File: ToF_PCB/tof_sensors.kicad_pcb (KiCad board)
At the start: 2 copper layers, 80 x 14 mm, 22 parts, among them J1 Conn_01x06, Q1 2N7002, Q2 2N7002, U1 LP5907MFX-2.8, U2 VL53L4CD, U3 VL53L4CD

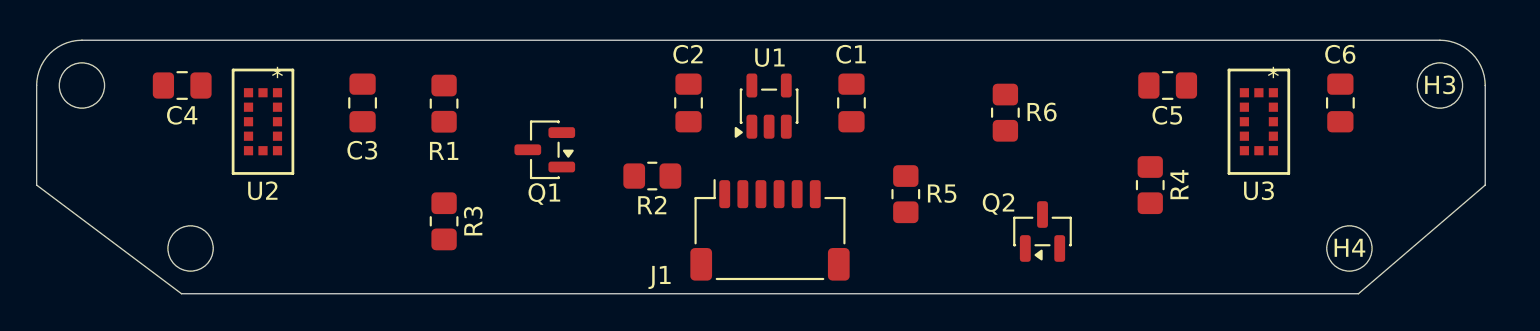
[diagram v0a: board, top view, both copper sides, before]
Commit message: Added layers and fixed layout + shape of pcb. Going to add esd protection now so pushing changes before doing so.
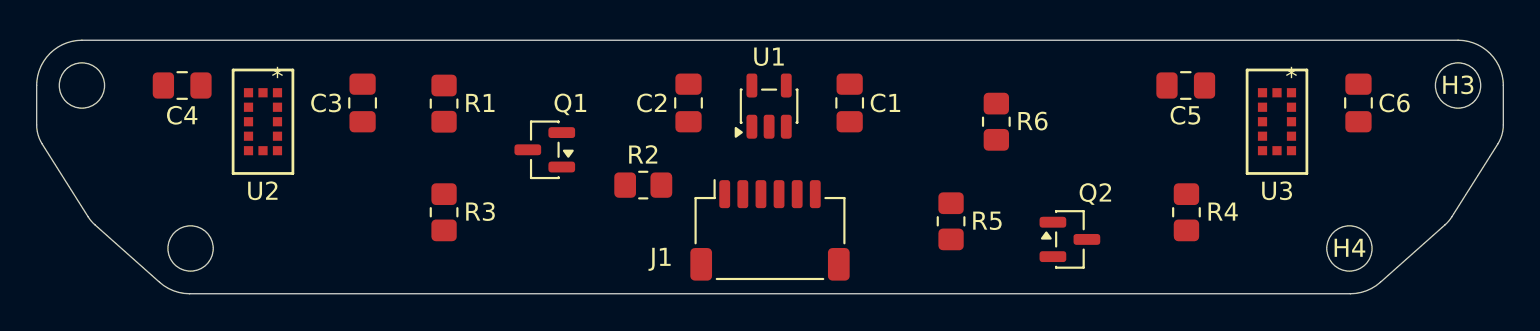
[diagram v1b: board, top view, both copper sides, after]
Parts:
- moved R5 2.92 mm to (132.0, 40.0)
- moved R4 2.50 mm to (145.0, 39.5)
- moved Q2 1.57 mm to (138.6, 41.0), turned to 0 degrees
- moved C5 1.00 mm to (145.0, 32.5)
- moved C6 1.00 mm to (154.5, 33.5)
- moved H3 1.00 mm to (160.0, 32.5)
- moved U3 1.00 mm to (150.0, 34.5)
- moved R2 0.71 mm to (115.0, 38.0)
- moved R6 0.71 mm to (134.5, 34.5), turned to 90 degrees
- moved R3 0.50 mm to (104.0, 39.5)
- moved C1 0.10 mm to (126.4, 33.5)
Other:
- board size 80 x 14 mm -> 81 x 14 mm
- copper layers 2 -> 4

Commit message: Updated pcb layout. Moved ToF sensors to back of board.
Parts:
- added C7: 100nF, Capacitor_SMD:C_0402_1005Metric, F.Cu at (126.3, 36.2)
- added U4: USBLC6-4SC6, Package_TO_SOT_SMD:SOT-23-6, F.Cu at (129.4, 36.3)
- C1, C2: footprint Capacitor_SMD:C_0805_2012Metric_Pad1.18x1.45mm_HandSolder -> Capacitor_SMD:C_0603_1608Metric_Pad1.08x0.95mm_HandSolder
- J1: footprint Connector_JST:JST_SH_SM06B-SRSS-TB_1x06-1MP_P1.00mm_Horizontal -> Connector_JST:JST_SH_BM06B-SRSS-TB_1x06-1MP_P1.00mm_Vertical
- U2, U3: moved to B.Cu
- moved R3 33.5 mm to (137.0, 33.5)
- moved R6 18.0 mm to (116.5, 33.5)
- moved R1 14.5 mm to (89.5, 32.5)
- moved C1 11.7 mm to (116.5, 39.9)
- moved Q1 11.5 mm to (99.0, 40.5)
- moved R2 10.9 mm to (104.4, 40.5), turned to -90 degrees
- moved C5 10.5 mm to (155.2, 34.5), turned to 0 degrees
- moved C4 10.0 mm to (99.5, 32.0), turned to 0 degrees
- moved U1 9.82 mm to (113.5, 38.7)
- moved J1 7.41 mm to (129.4, 41.3), turned to 180 degrees
- moved R4 7.07 mm to (144.0, 32.5), turned to 0 degrees
- moved C2 6.37 mm to (111.5, 35.6), turned to 180 degrees
- moved R5 6.00 mm to (138.0, 40.0), turned to 0 degrees
- moved Q2 4.88 mm to (143.4, 41.0)
- moved C6 1.64 mm to (155.2, 32.0), turned to 0 degrees
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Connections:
- net Net-(Q1-D) renamed /LEFT_XSHUT
- net Net-(Q2-D) renamed /RIGHT_XSHUT
- J1 pad 1: +3.3V -> GND
- J1 pad 2: /TOF_LEFT_DISABLE -> /TOF_RIGHT_DISABLE
- J1 pad 5: /TOF_RIGHT_DISABLE -> /TOF_LEFT_DISABLE
- J1 pad 6: GND -> +3.3V
